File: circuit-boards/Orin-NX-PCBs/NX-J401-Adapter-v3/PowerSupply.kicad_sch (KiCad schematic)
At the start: 23 parts, among them Q4 CSD16322Q5, Q5 SI4483ADY-T1-GE3, U1 LM3478MA

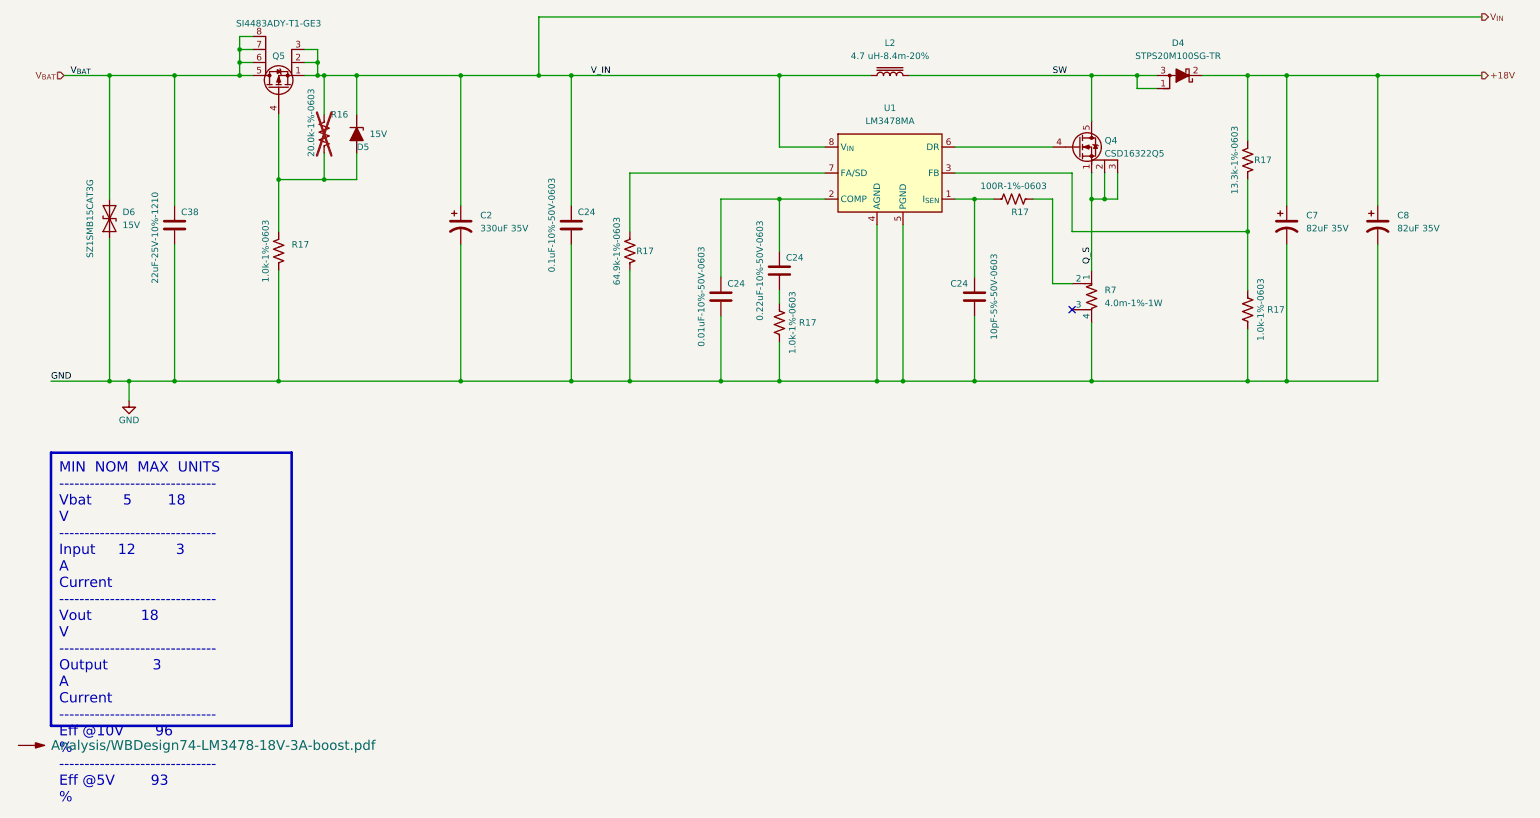
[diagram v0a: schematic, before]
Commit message: NX Adapter interim checking
Signed-off-by: Scott <sgberman1@gmail.com>
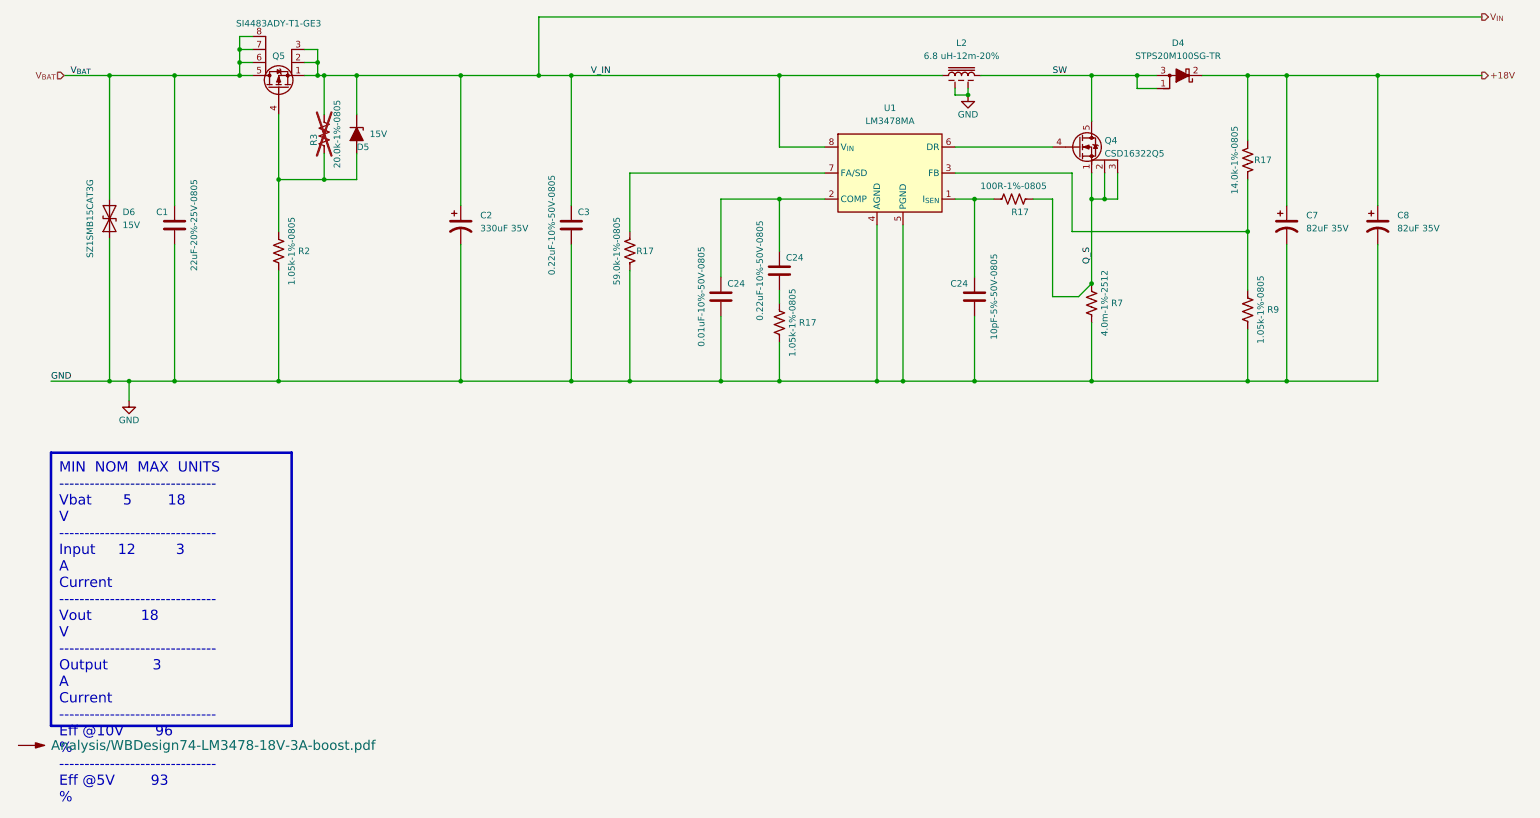
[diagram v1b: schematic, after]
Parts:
- removed C24: 0.1uF-10%-50V-0603, Capacitor_SMD:C_0603_1608Metric, symbol Device:C
- removed C38: 22uF-25V-10%-1210, Capacitor_SMD:C_1210_3225Metric, symbol Device:C
- removed R16: 20.0k-1%-0603, Resistor_SMD:R_0603_1608Metric, symbol Device:R_US
- removed R17 (x2): 1.0k-1%-0603, Resistor_SMD:R_0603_1608Metric, symbol Device:R_US
- removed R7: 4.0m-1%-1W, Resistor_SMD:R_Shunt_Vishay_WSKW0612, symbol Device:R_Shunt_US
- added C1: 22uF-20%-25V-0805, Capacitor_SMD:C_0805_2012Metric, symbol Device:C
- added C3: 0.22uF-10%-50V-0805, Capacitor_SMD:C_0805_2012Metric, symbol Device:C
- added R2, R9: 1.05k-1%-0805, Resistor_SMD:R_0805_2012Metric, symbol Device:R_US
- added R3: 20.0k-1%-0805, Resistor_SMD:R_0805_2012Metric, symbol Device:R_US
- added R7: 4.0m-1%-2512, Resistor_SMD:R_2512_6332Metric, symbol Device:R_US
- C24: value 10pF-5%-50V-0603 -> 10pF-5%-50V-0805; footprint Capacitor_SMD:C_0603_1608Metric -> Capacitor_SMD:C_0805_2012Metric; DIST P/N 478-KGM15ACG1H100JTCT-ND -> 1276-2561-1-ND; MFG KYOCERA AVX -> Samsung Electro-Mechanics; MFG P/N KGM15ACG1H100JT -> CL21C100CBANNNC
- C24: value 0.01uF-10%-50V-0603 -> 0.01uF-10%-50V-0805; footprint Capacitor_SMD:C_0603_1608Metric -> Capacitor_SMD:C_0805_2012Metric; DIST P/N 1276-1009-1-ND -> 1276-1015-1-ND; MFG P/N CL10B103KB8NNNC -> CL21B103KBANNNC
- C24: value 0.22uF-10%-50V-0603 -> 0.22uF-10%-50V-0805; footprint Capacitor_SMD:C_0603_1608Metric -> Capacitor_SMD:C_0805_2012Metric; DIST P/N 1276-6600-1-ND -> 399-C0805C224K5RACTUCT-ND; MFG Samsung Electro-Mechanics -> KEMET; MFG P/N CL10B224KB8VPNC -> C0805C224K5RAC7800
- L2: value 4.7 uH-8.4m-20% -> 6.8 uH-12m-20%; footprint NX-J401-Adapter:Bourns-SRP1265A -> NX-J401-Adapter:INDUCTOR_IHLE-5050FH-Vishay; DIST P/N SRP1265A-4R7MCT-ND -> 541-IHLE5050FHER6R8M5ACT-ND; MFG Bourns -> Vishay Dale; MFG P/N SRP1265A-4R7M -> IHLE5050FHER6R8M5A
- R17: value 1.0k-1%-0603 -> 1.05k-1%-0805; footprint Resistor_SMD:R_0603_1608Metric -> Resistor_SMD:R_0805_2012Metric; DIST P/N 311-1.00KHRCT-ND -> 311-1.05KCRCT-ND; MFG P/N RC0603FR-071KL -> RC0805FR-071K05L
- R17: value 64.9k-1%-0603 -> 59.0k-1%-0805; footprint Resistor_SMD:R_0603_1608Metric -> Resistor_SMD:R_0805_2012Metric; DIST P/N 311-64.9KHRCT-ND -> 311-59.0KCRCT-ND; MFG P/N RC0603FR-0764K9L -> RC0805FR-0759KL
- R17: value 100R-1%-0603 -> 100R-1%-0805; footprint Resistor_SMD:R_0603_1608Metric -> Resistor_SMD:R_0805_2012Metric; DIST P/N 311-100HRCT-ND -> 311-100CRCT-ND; MFG P/N RC0603FR-07100RL -> RC0805FR-07100RL
- R17: value 13.3k-1%-0603 -> 14.0k-1%-0805; footprint Resistor_SMD:R_0603_1608Metric -> Resistor_SMD:R_0805_2012Metric; DIST P/N 311-13.3KHRCT-ND -> 311-14.0KCRCT-ND; MFG P/N RC0603FR-0713K3L -> RC0805FR-0714KL
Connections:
- net GND: now also L2.3, L2.4, C1.2, C3.2, R2.1, R7.1, R9.1
- net Q_S: now also R17.1, R7.2
- net V_{BAT}: now also C1.1
- net V_{IN}: now also C3.1, R3.2
- net at D5.2 (A), Q5.4 (G): now also R2.2, R3.1
- net at R17.1, U1.3 (FB): now also R9.2
- no-connect marks 1 -> 0

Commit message: Check in of NX Adapter and Indicator boards.  Complete pending review
Signed-off-by: Scott <sgberman1@gmail.com>
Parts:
- C1: renamed from C8; DIST Mouser -> Digikey; DIST P/N 667-35SEPF82M -> P16345-ND
- C2: renamed from C7; DIST Mouser -> Digikey; DIST P/N 667-35SEPF82M -> P16345-ND
- Q5: DIST Mouser -> Digikey; DIST P/N 781-SI4483ADY-GE3 -> SI4483ADY-T1-GE3CT-ND
- R6: renamed from R3; DIST (none) -> Digikey; DIST P/N (none) -> 311-20.0KCRCT-ND; MFG (none) -> Yageo; MFG P/N (none) -> RC0805FR-0720KL
- renumbered C2 to C13, C3 to C5, C1 to C6, D4 to D3, R7 to R2, R2 to R5, R9 to R8, U1 to U2
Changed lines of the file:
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@@
 		(on_board yes)
 		(dnp no)
-		(property "Reference" "R2"
+		(property "Reference" "R5"
 			(at 95.25 105.41 0)
 			(effects
@@
 			)
 		)
-		(property "Datasheet" "~"
+		(property "Datasheet" "Components/YageoPYu-RC_Group_51_RoHS_L_12.pdf"
 			(at 91.44 105.41 0)
 			(effects
@@
 			(project "NX-J401-Adapter"
 				(path "/cc31ce4b-09ab-4aea-a1d3-ed84696ba658/584f7d71-5922-4ce5-8f88-d664ca9e2a8c"
-					(reference "R2")
+					(reference "R5")
 					(unit 1)
 				)
@@
 			)
 		)
-		(property "Datasheet" "~"
+		(property "Datasheet" "Components/YageoPYu-RC_Group_51_RoHS_L_12.pdf"
 			(at 189.23 119.38 0)
 			(effects
@@
 			(project "NX-J401-Adapter"
 				(path "/cc31ce4b-09ab-4aea-a1d3-ed84696ba658/584f7d71-5922-4ce5-8f88-d664ca9e2a8c"
-					(reference "R5")
+					(reference "R9")
 					(unit 1)
 				)
@@
 			(project "NX-J401-Adapter"
 				(path "/cc31ce4b-09ab-4aea-a1d3-ed84696ba658/584f7d71-5922-4ce5-8f88-d664ca9e2a8c"
-					(reference "C6")
+					(reference "C7")
 					(unit 1)
 				)
@@
 		(dnp no)
 		(fields_autoplaced yes)
-		(property "Reference" "C8"
+		(property "Reference" "C1"
 			(at 309.88 98.425 0)
 			(effects
@@
 			)
 		)
-		(property "Datasheet" "https://industrial.panasonic.com/ww/products/pt/os-con/models/35SEPF82M"
+		(property "Datasheet" "Components/Panasonic-AAB8000C250.pdf"
 			(at 306.07 100.33 0)
 			(effects
@@
 			)
 		)
-		(property "DIST" "Mouser"
+		(property "DIST" "Digikey"
 			(at 306.07 100.33 0)
 			(effects
@@
 			)
 		)
-		(property "DIST P/N" "667-35SEPF82M"
+		(property "DIST P/N" "P16345-ND"
 			(at 306.07 100.33 0)
 			(effects
@@
 			(project "NX-J401-Adapter"
 				(path "/cc31ce4b-09ab-4aea-a1d3-ed84696ba658/584f7d71-5922-4ce5-8f88-d664ca9e2a8c"
-					(reference "C8")
+					(reference "C1")
 					(unit 1)
 				)
@@
 			(project "NX-J401-Adapter"
 				(path "/cc31ce4b-09ab-4aea-a1d3-ed84696ba658/584f7d71-5922-4ce5-8f88-d664ca9e2a8c"
-					(reference "Q2")
+					(reference "Q1")
 					(unit 1)
 				)
@@
 			)
 		)
-		(property "Datasheet" "~"
+		(property "Datasheet" "Components/YageoPYu-RC_Group_51_RoHS_L_12.pdf"
 			(at 160.02 105.41 0)
 			(effects
@@
 			(project "NX-J401-Adapter"
 				(path "/cc31ce4b-09ab-4aea-a1d3-ed84696ba658/584f7d71-5922-4ce5-8f88-d664ca9e2a8c"
-					(reference "R4")
+					(reference "R3")
 					(unit 1)
 				)
@@
 		(dnp no)
 		(fields_autoplaced yes)
-		(property "Reference" "C7"
+		(property "Reference" "C2"
 			(at 292.1 98.425 0)
 			(effects
@@
 			)
 		)
-		(property "Datasheet" "https://industrial.panasonic.com/ww/products/pt/os-con/models/35SEPF82M"
+		(property "Datasheet" "Components/Panasonic-AAB8000C250.pdf"
 			(at 288.29 100.33 0)
 			(effects
@@
 			)
 		)
-		(property "DIST" "Mouser"
+		(property "DIST" "Digikey"
 			(at 288.29 100.33 0)
 			(effects
@@
 			)
 		)
-		(property "DIST P/N" "667-35SEPF82M"
+		(property "DIST P/N" "P16345-ND"
 			(at 288.29 100.33 0)
 			(effects
@@
 			(project "NX-J401-Adapter"
 				(path "/cc31ce4b-09ab-4aea-a1d3-ed84696ba658/584f7d71-5922-4ce5-8f88-d664ca9e2a8c"
-					(reference "C7")
+					(reference "C2")
 					(unit 1)
 				)
@@
 			(project "NX-J401-Adapter"
 				(path "/cc31ce4b-09ab-4aea-a1d3-ed84696ba658/584f7d71-5922-4ce5-8f88-d664ca9e2a8c"
-					(reference "C4")
+					(reference "C11")
 					(unit 1)
 				)
@@
 			)
 		)
-		(property "Datasheet" "~"
+		(property "Datasheet" "Components/YageoPYu-RC_Group_51_RoHS_L_12.pdf"
 			(at 234.95 95.25 0)
 			(effects
@@
 			(project "NX-J401-Adapter"
 				(path "/cc31ce4b-09ab-4aea-a1d3-ed84696ba658/584f7d71-5922-4ce5-8f88-d664ca9e2a8c"
-					(reference "R6")
+					(reference "R4")
 					(unit 1)
 				)
@@
 			)
 		)
-		(property "Datasheet" "https://www.vishay.com/docs/68982/si4483ad.pdf"
+		(property "Datasheet" "Components/Vishay-si4483ad.pdf"
 			(at 91.44 73.66 0)
 			(effects
@@
 			)
 		)
-		(property "DIST" "Mouser"
+		(property "DIST" "Digikey"
 			(at 91.44 73.66 90)
 			(effects
@@
 			)
 		)
-		(property "DIST P/N" "781-SI4483ADY-GE3"
+		(property "DIST P/N" "SI4483ADY-T1-GE3CT-ND"
 			(at 91.44 73.66 90)
 			(effects
@@
 			(project "NX-J401-Adapter"
 				(path "/cc31ce4b-09ab-4aea-a1d3-ed84696ba658/584f7d71-5922-4ce5-8f88-d664ca9e2a8c"
-					(reference "Q1")
+					(reference "Q2")
 					(unit 1)
 				)
@@
 		(on_board yes)
 		(dnp no)
-		(property "Reference" "C3"
+		(property "Reference" "C5"
 			(at 149.86 97.79 0)
 			(effects
@@
 			)
 		)
-		(property "Datasheet" "~"
+		(property "Datasheet" "Components/KEMET_C1002_X7R_SMD.pdf"
 			(at 148.59 100.33 0)
 			(effects
@@
 			(project "NX-J401-Adapter"
 				(path "/cc31ce4b-09ab-4aea-a1d3-ed84696ba658/584f7d71-5922-4ce5-8f88-d664ca9e2a8c"
-					(reference "C3")
+					(reference "C5")
 					(unit 1)
 				)
@@
 		(dnp no)
 		(fields_autoplaced yes)
-		(property "Reference" "C2"
+		(property "Reference" "C13"
 			(at 130.81 98.425 0)
 			(effects
@@
 			)
 		)
-		(property "Datasheet" "https://www.rubycon.co.jp/wp-content/uploads/catalog-hybrid/PZJ.pdf"
+		(property "Datasheet" "Components/Rubicon-PZJ.pdf"
 			(at 127 100.33 0)
 			(effects
@@
 			(project "NX-J401-Adapter"
 				(path "/cc31ce4b-09ab-4aea-a1d3-ed84696ba658/584f7d71-5922-4ce5-8f88-d664ca9e2a8c"
-					(reference "C2")
+					(reference "C13")
 					(unit 1)
 				)
@@
 			)
 		)
-		(property "Datasheet" "~"
+		(property "Datasheet" "Components/Nexperia-BZT52H_SER.pdf"
 			(at 106.68 82.55 0)
 			(effects
@@
 			(project "NX-J401-Adapter"
 				(path "/cc31ce4b-09ab-4aea-a1d3-ed84696ba658/584f7d71-5922-4ce5-8f88-d664ca9e2a8c"
-					(reference "D3")
+					(reference "D5")
 					(unit 1)
 				)
@@
 		(on_board yes)
 		(dnp no)
-		(property "Reference" "R9"
+		(property "Reference" "R8"
 			(at 284.48 116.84 0)
 			(effects
@@
 			)
 		)
-		(property "Datasheet" "~"
+		(property "Datasheet" "Components/YageoPYu-RC_Group_51_RoHS_L_12.pdf"
 			(at 280.67 116.84 0)
 			(effects
@@
 			(project "NX-J401-Adapter"
 				(path "/cc31ce4b-09ab-4aea-a1d3-ed84696ba658/584f7d71-5922-4ce5-8f88-d664ca9e2a8c"
-					(reference "R9")
+					(reference "R8")
 					(unit 1)
 				)
@@
 			)
 		)
-		(property "Datasheet" "~"
+		(property "Datasheet" "Components/YageoPYu-RC_Group_51_RoHS_L_12.pdf"
 			(at 280.67 87.63 0)
 			(effects
@@
 			(project "NX-J401-Adapter"
 				(path "/cc31ce4b-09ab-4aea-a1d3-ed84696ba658/584f7d71-5922-4ce5-8f88-d664ca9e2a8c"
-					(reference "R8")
+					(reference "R7")
 					(unit 1)
 				)
@@
 		(on_board yes)
 		(dnp no)
-		(property "Reference" "C1"
+		(property "Reference" "C6"
 			(at 69.85 97.79 0)
 			(effects
@@
 			(project "NX-J401-Adapter"
 				(path "/cc31ce4b-09ab-4aea-a1d3-ed84696ba658/584f7d71-5922-4ce5-8f88-d664ca9e2a8c"
-					(reference "C1")
+					(reference "C6")
 					(unit 1)
 				)
@@
 			(project "NX-J401-Adapter"
 				(path "/cc31ce4b-09ab-4aea-a1d3-ed84696ba658/584f7d71-5922-4ce5-8f88-d664ca9e2a8c"
-					(reference "L1")
+					(reference "L2")
 					(unit 1)
 				)
@@
 		(on_board yes)
 		(dnp no)
-		(property "Reference" "R7"
+		(property "Reference" "R2"
 			(at 254 115.57 0)
 			(effects
@@
 			)
 		)
-		(property "Datasheet" "~"
+		(property "Datasheet" "Components/Bourns-cre.pdf"
 			(at 250.19 115.57 0)
 			(effects
@@
 			(project "NX-J401-Adapter"
 				(path "/cc31ce4b-09ab-4aea-a1d3-ed84696ba658/584f7d71-5922-4ce5-8f88-d664ca9e2a8c"
-					(reference "R7")
+					(reference "R2")
 					(unit 1)
 				)
@@
 		(on_board yes)
 		(dnp yes)
-		(property "Reference" "R3"
+		(property "Reference" "R6"
 			(at 98.298 84.836 90)
 			(effects
@@
 			)
 		)
-		(property "Datasheet" "~"
+		(property "Datasheet" "Components/YageoPYu-RC_Group_51_RoHS_L_12.pdf"
 			(at 100.33 82.55 0)
 			(effects
@@
 			)
 		)
-		(property "MFG" ""
+		(property "MFG" "Yageo"
 			(at 100.33 82.55 0)
 			(effects
@@
 			)
 		)
-		(property "MFG P/N" ""
+		(property "MFG P/N" "RC0805FR-0720KL"
 			(at 100.33 82.55 0)
 			(effects
@@
 			)
 		)
-		(property "DIST" ""
+		(property "DIST" "Digikey"
 			(at 100.33 82.55 0)
 			(effects
@@
 			)
 		)
-		(property "DIST P/N" ""
+		(property "DIST P/N" "311-20.0KCRCT-ND"
 			(at 100.33 82.55 0)
 			(effects
@@
 			(project "NX-J401-Adapter"
 				(path "/cc31ce4b-09ab-4aea-a1d3-ed84696ba658/584f7d71-5922-4ce5-8f88-d664ca9e2a8c"
-					(reference "R3")
+					(reference "R6")
 					(unit 1)
 				)
@@
 		(dnp no)
 		(fields_autoplaced yes)
-		(property "Reference" "D4"
+		(property "Reference" "D3"
 			(at 267.081 64.77 0)
 			(effects
@@
 			(project "NX-J401-Adapter"
 				(path "/cc31ce4b-09ab-4aea-a1d3-ed84696ba658/584f7d71-5922-4ce5-8f88-d664ca9e2a8c"
-					(reference "D4")
+					(reference "D3")
 					(unit 1)
 				)
@@
 		(dnp no)
 		(fields_autoplaced yes)
-		(property "Reference" "U1"
+		(property "Reference" "U2"
 			(at 210.82 77.47 0)
 			(effects
@@
 			)
 		)
-		(property "Datasheet" "https://www.ti.com/lit/gpn/lm3478"
+		(property "Datasheet" "Components/TI-lm3478.pdf"
 			(at 211.455 77.47 0)
 			(effects
@@
 			(project "NX-J401-Adapter"
 				(path "/cc31ce4b-09ab-4aea-a1d3-ed84696ba658/584f7d71-5922-4ce5-8f88-d664ca9e2a8c"
-					(reference "U1")
+					(reference "U2")
 					(unit 1)
 				)
@@
 			)
 		)
-		(property "Datasheet" "~"
+		(property "Datasheet" "Components/KEMET_C1002_X7R_SMD.pdf"
 			(at 189.23 109.22 0)
 			(effects
@@
 			(project "NX-J401-Adapter"
 				(path "/cc31ce4b-09ab-4aea-a1d3-ed84696ba658/584f7d71-5922-4ce5-8f88-d664ca9e2a8c"
-					(reference "C5")
+					(reference "C12")
 					(unit 1)
 				)
@@
 			(project "NX-J401-Adapter"
 				(path "/cc31ce4b-09ab-4aea-a1d3-ed84696ba658/584f7d71-5922-4ce5-8f88-d664ca9e2a8c"
-					(reference "D2")
-					(unit 1)
-				)
+					(reference "D4")
+					(unit 1)
+				)

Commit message: Update power supply inductor to 4.7uF
Signed-off-by: Scott <sgberman1@gmail.com>
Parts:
- L2: value 6.8 uH-12m-20% -> 4.7 uH-8m-20%; DIST Digikey -> Mouser; DIST P/N 541-IHLE5050FHER6R8M5ACT-ND -> 70-IHLE5050FHR4R7M5A; MFG P/N IHLE5050FHER6R8M5A -> IHLE5050FHER4R7M5A
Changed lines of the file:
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@@
 		)
 	)
-	(text_box "          MIN  NOM  MAX  UNITS\n-------------------------------\nVbat       5        18     V\n-------------------------------\nInput     12         3     A\nCurrent\n-------------------------------\nVout           18          V\n-------------------------------\nOutput          3          A\nCurrent\n-------------------------------\nEff @10V       96          %\n-------------------------------\nEff @5V        93          %\n"
+	(text_box "          MIN  NOM  MAX  UNITS\n-------------------------------\nVbat       5        18     V\n-------------------------------\nInput     12         3     A\nCurrent\n-------------------------------\nVout           18          V\n-------------------------------\nOutput          3          A\nCurrent\n-------------------------------\nEff @10V       95.5          %\n-------------------------------\nEff @5V        92          %\n"
 		(exclude_from_sim no)
 		(at 46.99 144.78 0)
@@
 			)
 		)
-		(property "Description" ""
+		(property "Description" "N-Channel 25 V 21A (Ta), 97A (Tc) 3.1W (Ta) Surface Mount 8-VSON-CLIP (5x6)"
 			(at 247.65 85.09 0)
 			(effects
@@
 			)
 		)
-		(property "Datasheet" "Analysis/WBDesign74-LM3478-18V-3A-boost.pdf"
+		(property "Datasheet" "Analysis/WBDesign84-LM3478-18V-3A-boost.pdf"
 			(at 46.99 201.93 0)
 			(effects
@@
 			)
 		)
-		(property "Value" "6.8 uH-12m-20%"
+		(property "Value" "4.7 uH-8m-20%"
 			(at 224.79 67.31 90)
 			(effects
@@
 			)
 		)
-		(property "Description" "6.8 µH Shielded Inductor 14.9 A 12.09mOhm Max Nonstandard"
+		(property "Description" "4.7 µH Shielded Inductor 18.5 A 7.93mOhm Max"
 			(at 224.79 71.12 0)
 			(effects
@@
 			)
 		)
-		(property "MFG P/N" "IHLE5050FHER6R8M5A"
+		(property "MFG P/N" "IHLE5050FHER4R7M5A "
 			(at 224.79 71.12 90)
 			(effects
@@
 			)
 		)
-		(property "DIST" "Digikey"
+		(property "DIST" "Mouser"
 			(at 224.79 71.12 90)
 			(effects
@@
 			)
 		)
-		(property "DIST P/N" "541-IHLE5050FHER6R8M5ACT-ND"
+		(property "DIST P/N" "70-IHLE5050FHR4R7M5A "
 			(at 224.79 71.12 90)
 			(effects
